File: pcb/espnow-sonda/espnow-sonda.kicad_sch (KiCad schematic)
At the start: 62 parts, among them J1 Conn_01x04_Pin, J2 Conn_01x04_Pin, U1 LTC6269xMS8E, U2 XC6206P251, U3 LMH6611, U4 XC6902N251

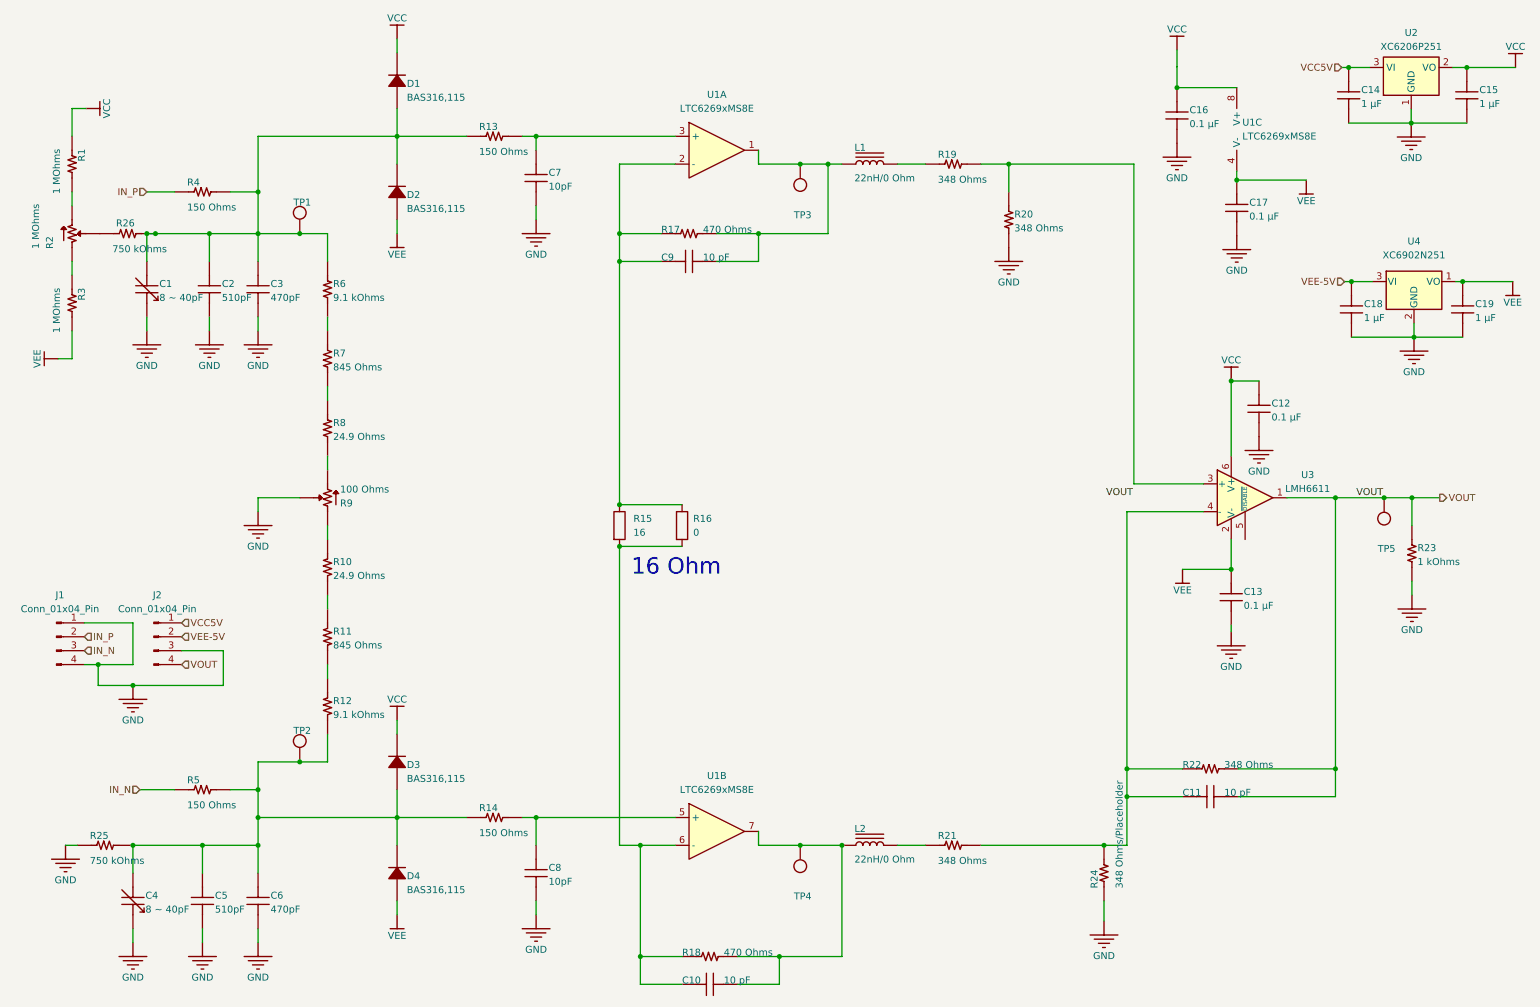
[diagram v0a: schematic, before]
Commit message: added simulation, updated pcb designs
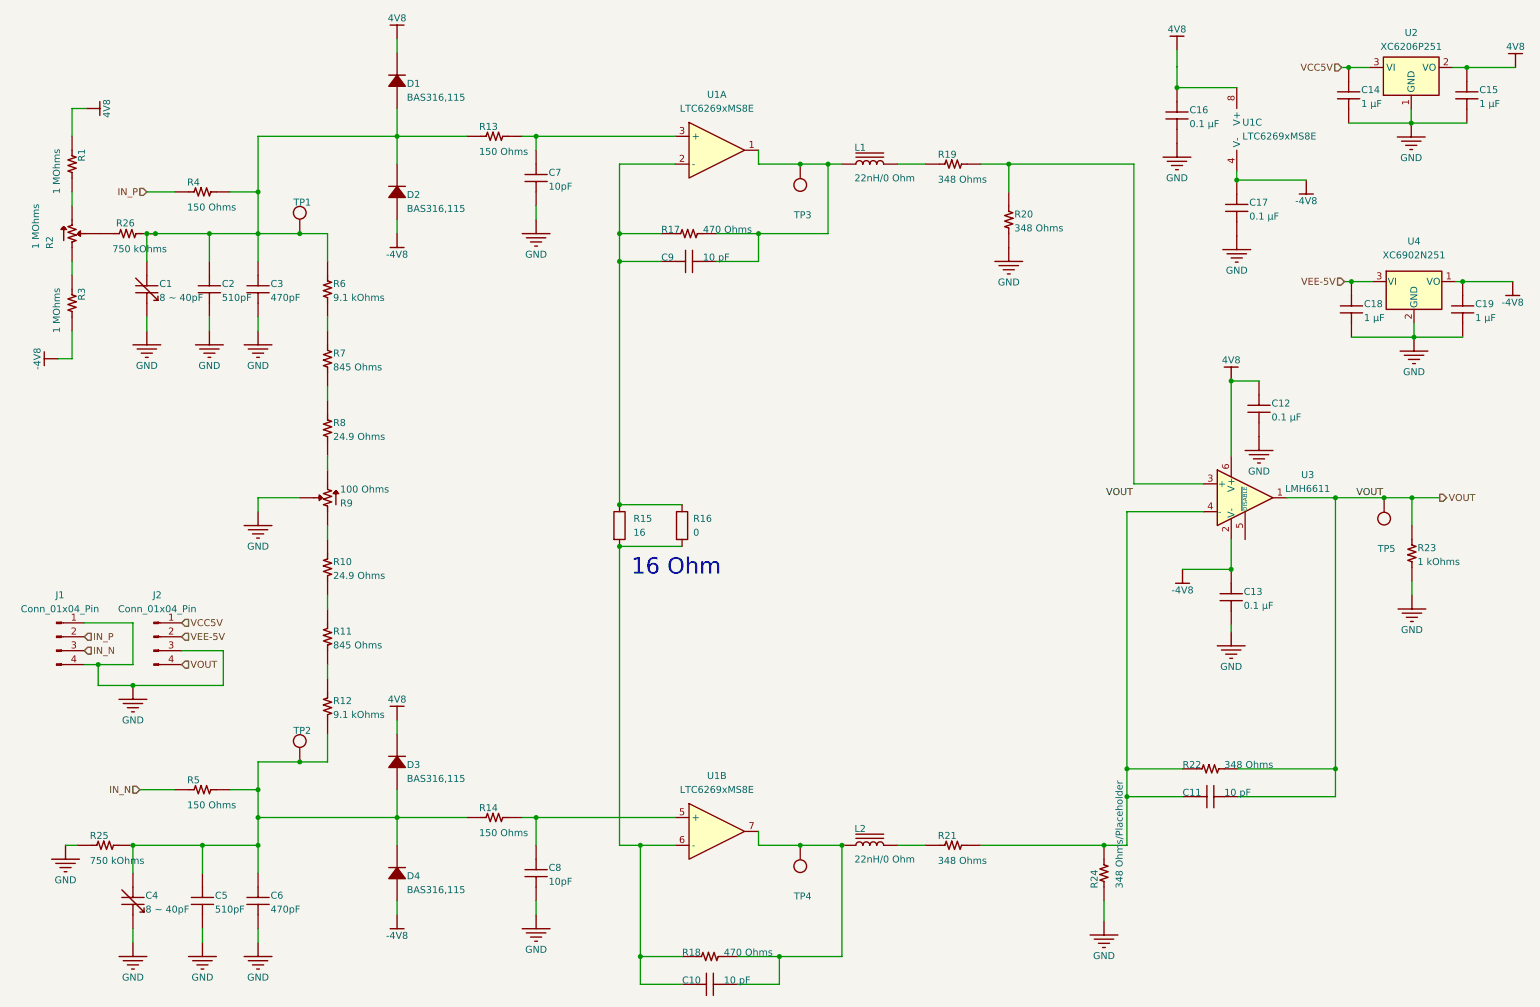
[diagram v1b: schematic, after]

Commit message: update sim symbol
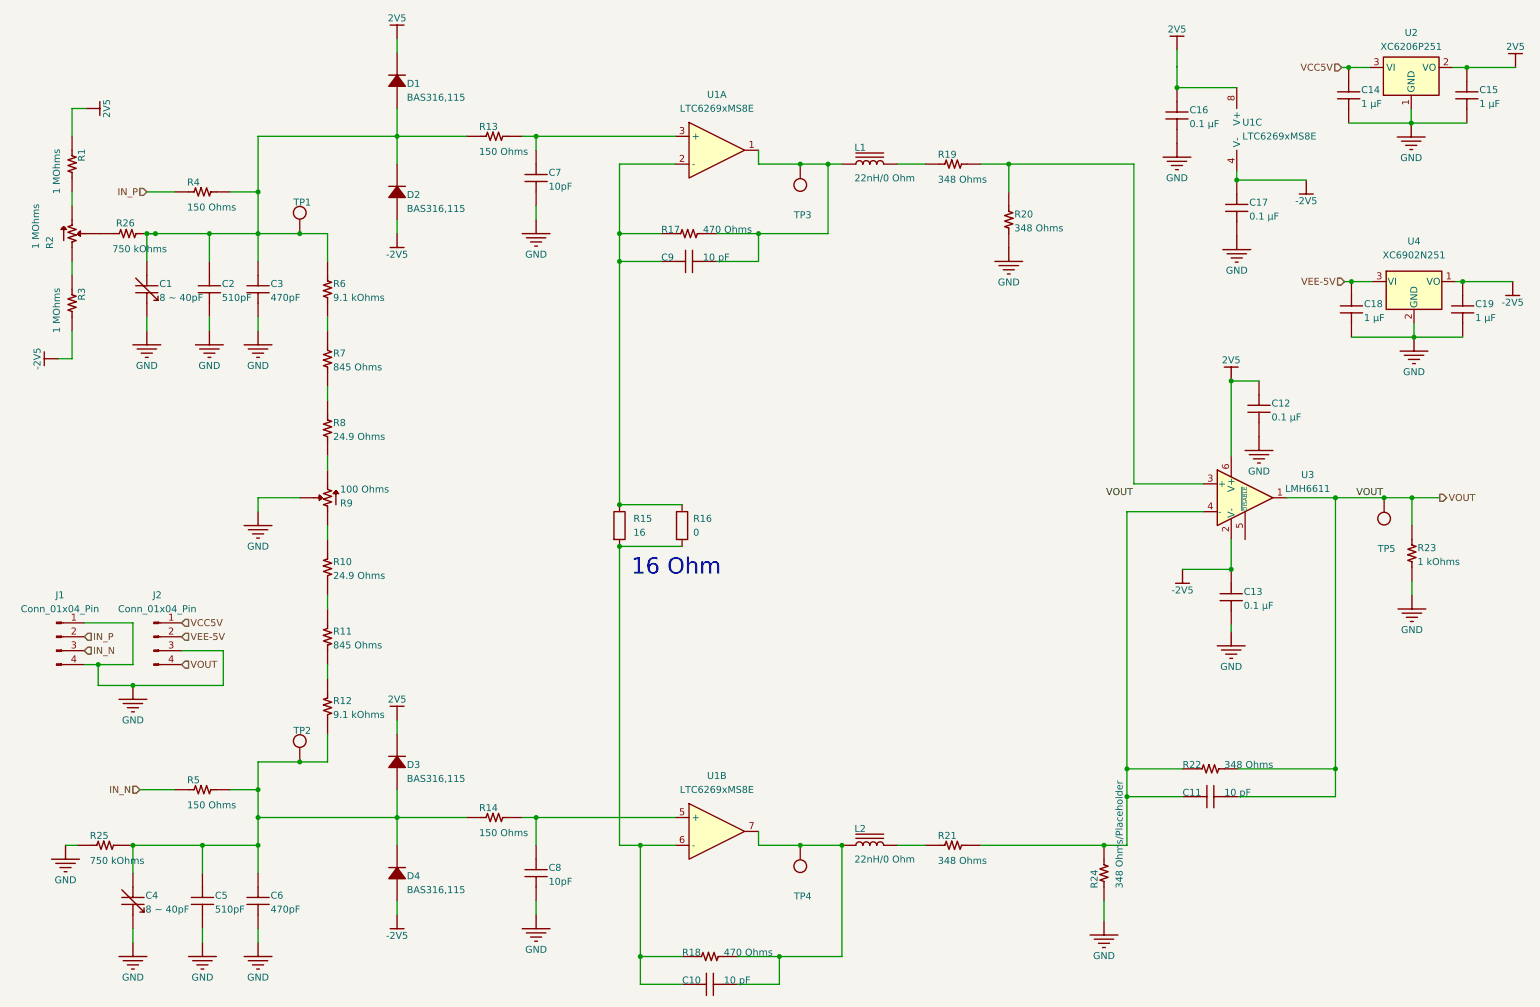
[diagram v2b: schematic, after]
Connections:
- net -4V8 renamed -2V5
- net 4V8 renamed 2V5
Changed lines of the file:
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@@
 (kicad_sch
-	(version 20231120)
+	(version 20250114)
 	(generator "eeschema")
-	(generator_version "8.0")
+	(generator_version "9.0")
 	(paper "A4")
+	(text "16 Ohm"
+		(exclude_from_sim no)
+		(at 119.507 115.824 0)
+		(effects
+			(font
+				(size 3 3)
+			)
+			(justify left bottom)
+		)
+	)
 	(junction
 		(at 102.108 35.306)
@@
 		)
 	)
-	(text "16 Ohm"
-		(exclude_from_sim no)
-		(at 119.507 115.824 0)
-		(effects
-			(font
-				(size 3 3)
-			)
-			(justify left bottom)
-		)
-	)
 	(label "VOUT"
 		(at 251.968 101.346 0)
@@
 			)
 		)
-		(property "Value" "4V8"
+		(property "Value" "2V5"
 			(at 23.6728 30.226 0)
 			(effects
@@
 			)
 		)
-		(property "Value" "-4V8"
+		(property "Value" "-2V5"
 			(at 76.708 181.356 0)
 			(effects
@@
 			)
 		)
-		(property "Value" "4V8"
+		(property "Value" "2V5"
 			(at 76.708 13.716 0)
 			(effects
@@
 			)
 		)
-		(property "Value" "-4V8"
+		(property "Value" "-2V5"
 			(at 76.708 56.896 0)
 			(effects
@@
 			)
 		)
-		(property "Value" "4V8"
+		(property "Value" "2V5"
 			(at 219.202 15.748 0)
 			(effects
@@
 			)
 		)
-		(property "Value" "4V8"
+		(property "Value" "2V5"
 			(at 229.108 76.2 0)
 			(effects
@@
 			)
 		)
-		(property "Value" "-4V8"
+		(property "Value" "-2V5"
 			(at 220.218 118.237 0)
 			(effects
@@
 			)
 		)
-		(property "Value" "4V8"
+		(property "Value" "2V5"
 			(at 281.051 18.923 0)
 			(effects
@@
 			)
 		)
-		(property "Value" "-4V8"
+		(property "Value" "-2V5"
 			(at 280.543 65.659 0)
 			(effects
@@
 			)
 		)
-		(property "Value" "-4V8"
+		(property "Value" "-2V5"
 			(at 242.824 47.117 0)
 			(effects
@@
 			)
 		)
-		(property "Value" "4V8"
+		(property "Value" "2V5"
 			(at 76.708 138.176 0)
 			(effects
@@
 			)
 		)
-		(property "Value" "-4V8"
+		(property "Value" "-2V5"
 			(at 10.9728 75.946 0)
 			(effects
@@
 		)
 	)
+	(embedded_fonts no)
 )
